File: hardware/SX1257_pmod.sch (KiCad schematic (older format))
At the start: 46 parts, among them J1 Conn_02x06_Odd_Even, J2 SMA_F_RX, J3 SMA_F_TX, U1 SX1257, U2 SC18IS602B, Y1 36MHz 10ppm

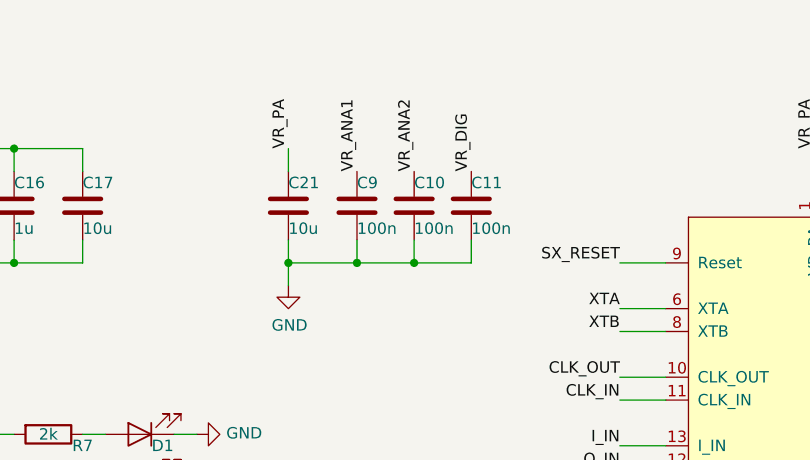
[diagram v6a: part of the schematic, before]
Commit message: Change C21 (VR_PA) to 10n
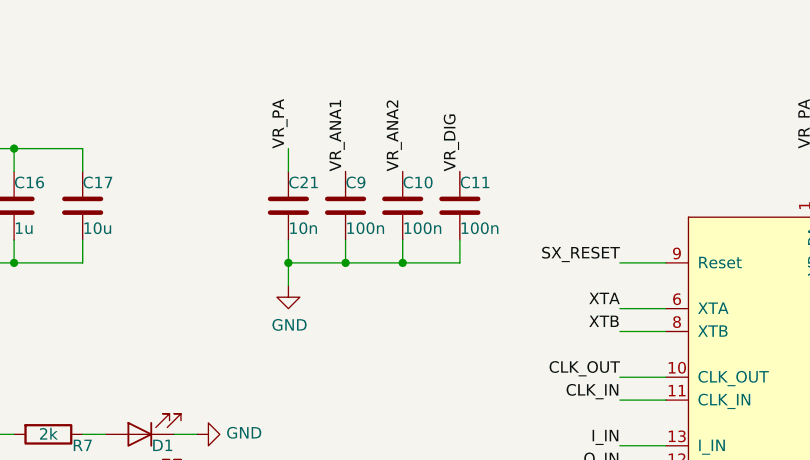
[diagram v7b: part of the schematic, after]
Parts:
- C21: value 10u -> 10n; footprint Capacitor_SMD:C_0603_1608Metric -> Capacitor_SMD:C_0402_1005Metric
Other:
- moved on the sheet: C10, C11, C9
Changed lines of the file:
@@
 L Device:C C9
 U 1 1 5C3393B3
-P 5400 1350
-F 0 "C9" H 5400 1450 50  0000 L CNN
-F 1 "100n" H 5400 1250 50  0000 L CNN
-F 2 "Capacitor_SMD:C_0402_1005Metric" H 5438 1200 50  0001 C CNN
-F 3 "~" H 5400 1350 50  0001 C CNN
-	1    5400 1350
+P 5350 1350
+F 0 "C9" H 5350 1450 50  0000 L CNN
+F 1 "100n" H 5350 1250 50  0000 L CNN
+F 2 "Capacitor_SMD:C_0402_1005Metric" H 5388 1200 50  0001 C CNN
+F 3 "~" H 5350 1350 50  0001 C CNN
+	1    5350 1350
 	1    0    0    -1
 $EndComp
@@
 L Device:C C10
 U 1 1 5C33942E
-P 5650 1350
-F 0 "C10" H 5650 1450 50  0000 L CNN
-F 1 "100n" H 5650 1250 50  0000 L CNN
-F 2 "Capacitor_SMD:C_0402_1005Metric" H 5688 1200 50  0001 C CNN
-F 3 "~" H 5650 1350 50  0001 C CNN
-	1    5650 1350
+P 5600 1350
+F 0 "C10" H 5600 1450 50  0000 L CNN
+F 1 "100n" H 5600 1250 50  0000 L CNN
+F 2 "Capacitor_SMD:C_0402_1005Metric" H 5638 1200 50  0001 C CNN
+F 3 "~" H 5600 1350 50  0001 C CNN
+	1    5600 1350
 	1    0    0    -1
 $EndComp
@@
 L Device:C C11
 U 1 1 5C339464
-P 5900 1350
-F 0 "C11" H 5900 1450 50  0000 L CNN
-F 1 "100n" H 5900 1250 50  0000 L CNN
-F 2 "Capacitor_SMD:C_0402_1005Metric" H 5938 1200 50  0001 C CNN
-F 3 "~" H 5900 1350 50  0001 C CNN
-	1    5900 1350
+P 5850 1350
+F 0 "C11" H 5850 1450 50  0000 L CNN
+F 1 "100n" H 5850 1250 50  0000 L CNN
+F 2 "Capacitor_SMD:C_0402_1005Metric" H 5888 1200 50  0001 C CNN
+F 3 "~" H 5850 1350 50  0001 C CNN
+	1    5850 1350
 	1    0    0    -1
 $EndComp
@@
 Wire Wire Line
 	7500 1100 7500 1300
-Text Label 5400 1200 1    50   ~ 0
+Text Label 5350 1200 1    50   ~ 0
 VR_ANA1
-Text Label 5650 1200 1    50   ~ 0
+Text Label 5600 1200 1    50   ~ 0
 VR_ANA2
-Text Label 5900 1200 1    50   ~ 0
+Text Label 5850 1200 1    50   ~ 0
 VR_DIG
 $Comp
@@
 	5100 1500 5100 1600
 Wire Wire Line
-	5100 1600 5400 1600
-Wire Wire Line
-	5400 1600 5400 1500
+	5100 1600 5350 1600
+Wire Wire Line
+	5350 1600 5350 1500
 Connection ~ 5100 1600
 Wire Wire Line
 	5100 1600 5100 1700
 Wire Wire Line
-	5400 1600 5650 1600
-Wire Wire Line
-	5650 1600 5650 1500
-Connection ~ 5400 1600
-Wire Wire Line
-	5650 1600 5900 1600
-Wire Wire Line
-	5900 1600 5900 1500
-Connection ~ 5650 1600
+	5350 1600 5600 1600
+Wire Wire Line
+	5600 1600 5600 1500
+Connection ~ 5350 1600
+Wire Wire Line
+	5600 1600 5850 1600
+Wire Wire Line
+	5850 1600 5850 1500
+Connection ~ 5600 1600
 $Comp
 L Device:C C21
@@
 P 5100 1350
 F 0 "C21" H 5100 1450 50  0000 L CNN
-F 1 "10u" H 5100 1250 50  0000 L CNN
-F 2 "Capacitor_SMD:C_0603_1608Metric" H 5138 1200 50  0001 C CNN
+F 1 "10n" H 5100 1250 50  0000 L CNN
+F 2 "Capacitor_SMD:C_0402_1005Metric" H 5138 1200 50  0001 C CNN
 F 3 "~" H 5100 1350 50  0001 C CNN
 	1    5100 1350

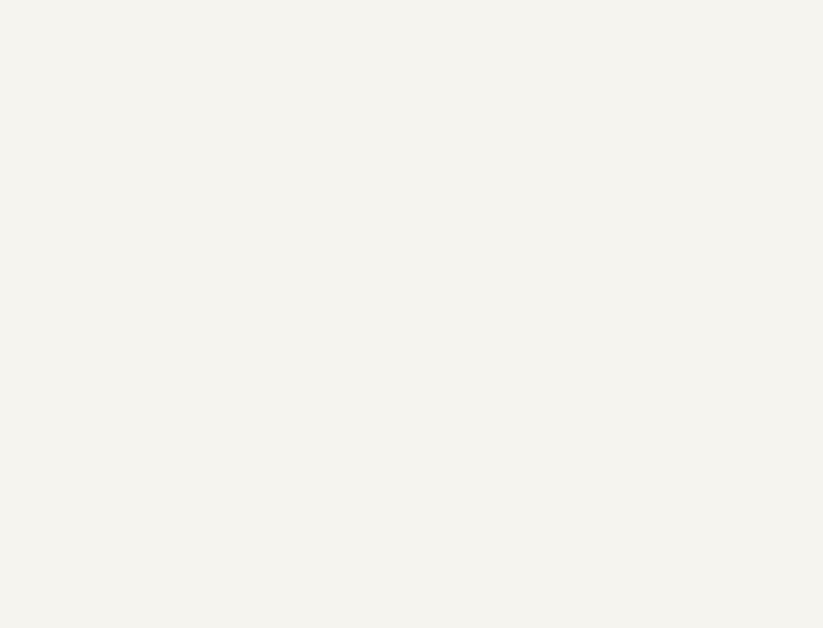
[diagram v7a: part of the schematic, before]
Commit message: Integrate SI514
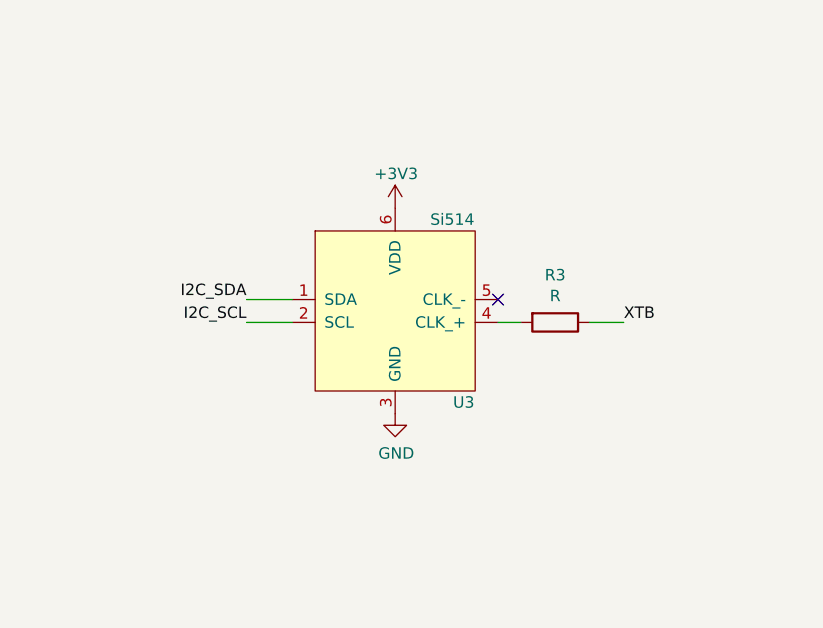
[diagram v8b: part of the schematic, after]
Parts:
- added R3: R, Resistor_SMD:R_0402_1005Metric, symbol Device:R
- added U3: Si514, extra:Oscillator_SMD_Silicon_Labs_3.2x5.0mm_P1.27mm-6pin_5.0x3.2mm, symbol Si514:Si514
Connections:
- net +3V3: now also U3.6 (VDD)
- net GND: now also U3.3 (GND)
- net I2C_SCL: now also U3.2 (SCL)
- net I2C_SDA: now also U3.1 (SDA)
- net XTB: now also R3.1
- new net: R3.2, U3.4 (CLK_+)
- no-connect marks 1 -> 2
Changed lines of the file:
@@
 Wire Wire Line
 	3200 1600 3500 1600
+$Comp
+L Si514:Si514 U3
+U 1 1 5E37915E
+P 12450 4650
+F 0 "U3" H 12750 4300 50  0000 C CNN
+F 1 "Si514" H 12700 5100 50  0000 C CNN
+F 2 "extra:Oscillator_SMD_Silicon_Labs_3.2x5.0mm_P1.27mm-6pin_5.0x3.2mm" H 12000 4750 50  0001 C CNN
+F 3 "" H 12000 4750 50  0001 C CNN
+	1    12450 4650
+	1    0    0    -1
+$EndComp
+Text Label 11800 4550 2    50   ~ 0
+I2C_SDA
+Text Label 11800 4650 2    50   ~ 0
+I2C_SCL
+Wire Wire Line
+	11800 4650 12000 4650
+Wire Wire Line
+	11800 4550 12000 4550
+$Comp
+L power:+3V3 #PWR0104
+U 1 1 5E392DB5
+P 12450 4150
+F 0 "#PWR0104" H 12450 4000 50  0001 C CNN
+F 1 "+3V3" H 12350 4300 50  0000 L CNN
+F 2 "" H 12450 4150 50  0001 C CNN
+F 3 "" H 12450 4150 50  0001 C CNN
+	1    12450 4150
+	-1   0    0    -1
+$EndComp
+$Comp
+L power:GND #PWR0105
+U 1 1 5E393209
+P 12450 5050
+F 0 "#PWR0105" H 12450 4800 50  0001 C CNN
+F 1 "GND" H 12455 4877 50  0000 C CNN
+F 2 "" H 12450 5050 50  0001 C CNN
+F 3 "" H 12450 5050 50  0001 C CNN
+	1    12450 5050
+	1    0    0    -1
+$EndComp
+NoConn ~ 12900 4550
+$Comp
+L Device:R R3
+U 1 1 5E39DBA9
+P 13150 4650
+F 0 "R3" V 12943 4650 50  0000 C CNN
+F 1 "R" V 13034 4650 50  0000 C CNN
+F 2 "Resistor_SMD:R_0402_1005Metric" V 13080 4650 50  0001 C CNN
+F 3 "~" H 13150 4650 50  0001 C CNN
+	1    13150 4650
+	0    1    1    0
+$EndComp
+Wire Wire Line
+	12900 4650 13000 4650
+Text Label 13450 4650 0    50   ~ 0
+XTB
+Wire Wire Line
+	13300 4650 13450 4650
 $EndSCHEMATC
